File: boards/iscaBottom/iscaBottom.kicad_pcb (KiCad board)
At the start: 2 copper layers, 178.5 x 157 mm, 44 parts, among them J1 CONN_01X36, J2 CONN_01X36, J3 CONN_01X36

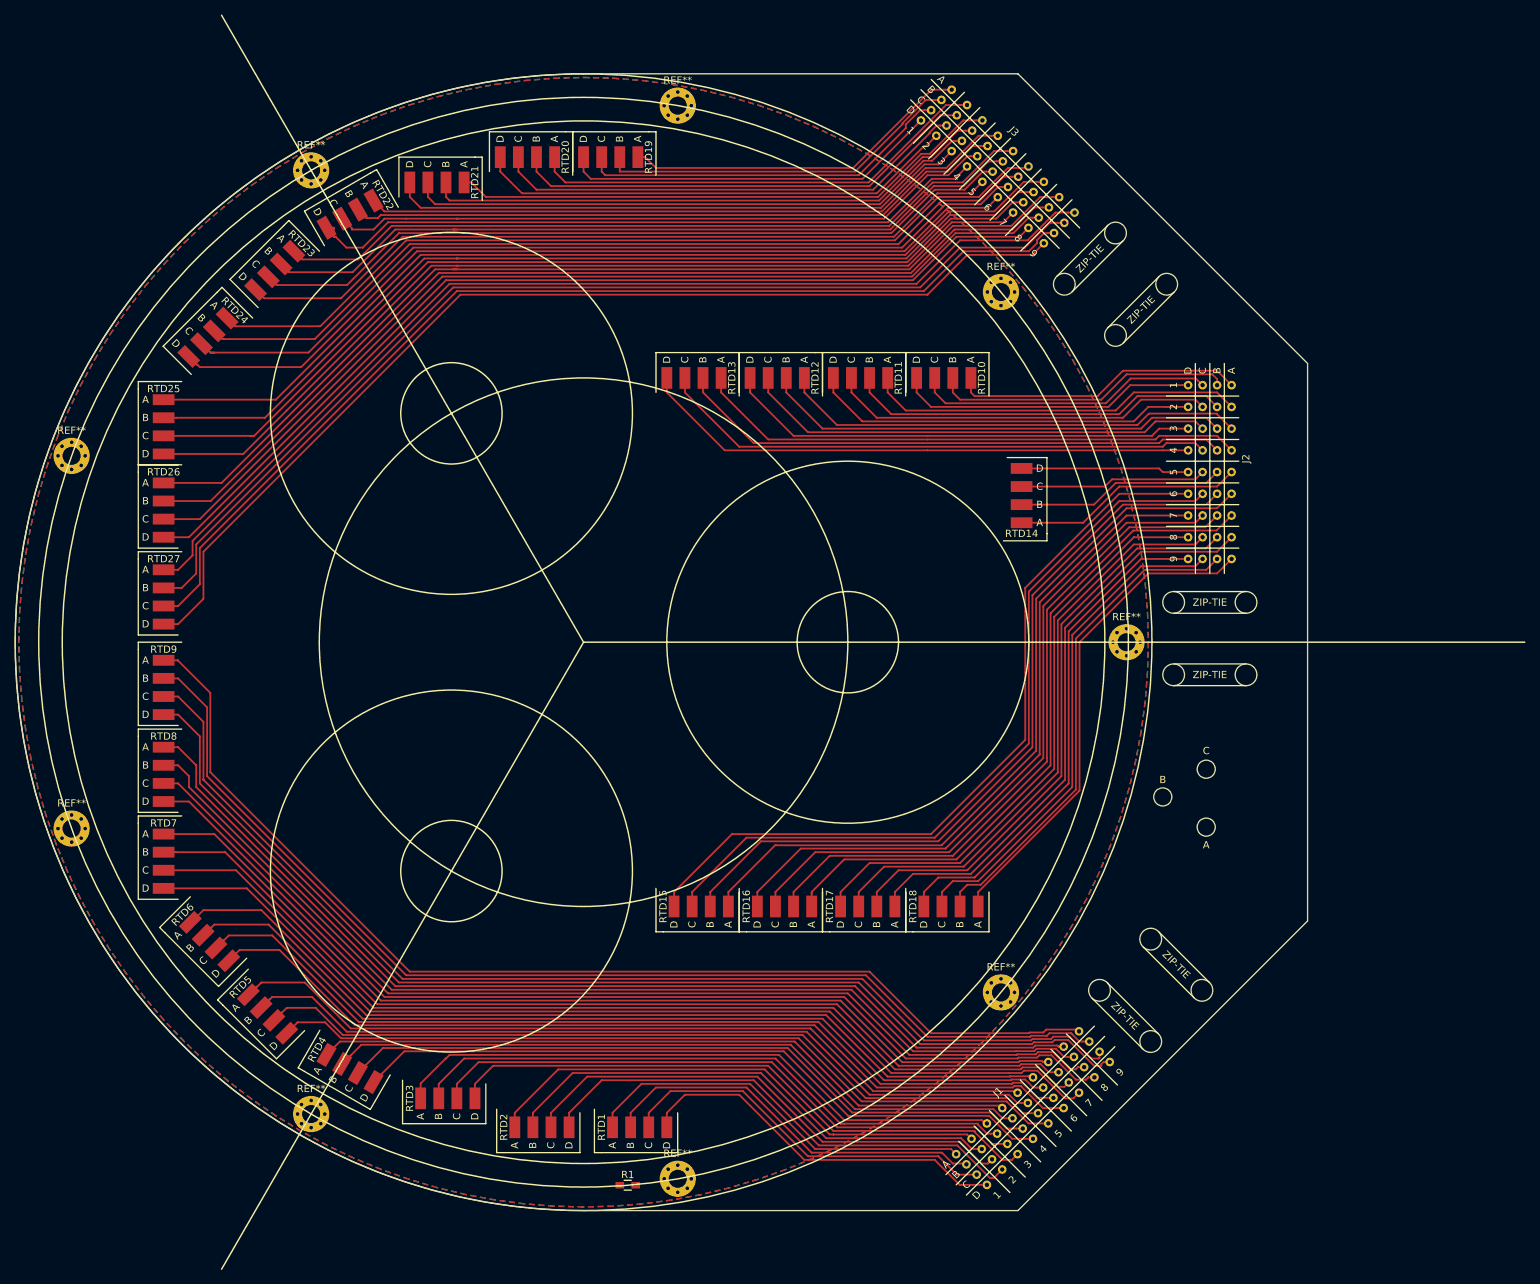
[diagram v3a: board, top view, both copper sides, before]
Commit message: addressed all the errors
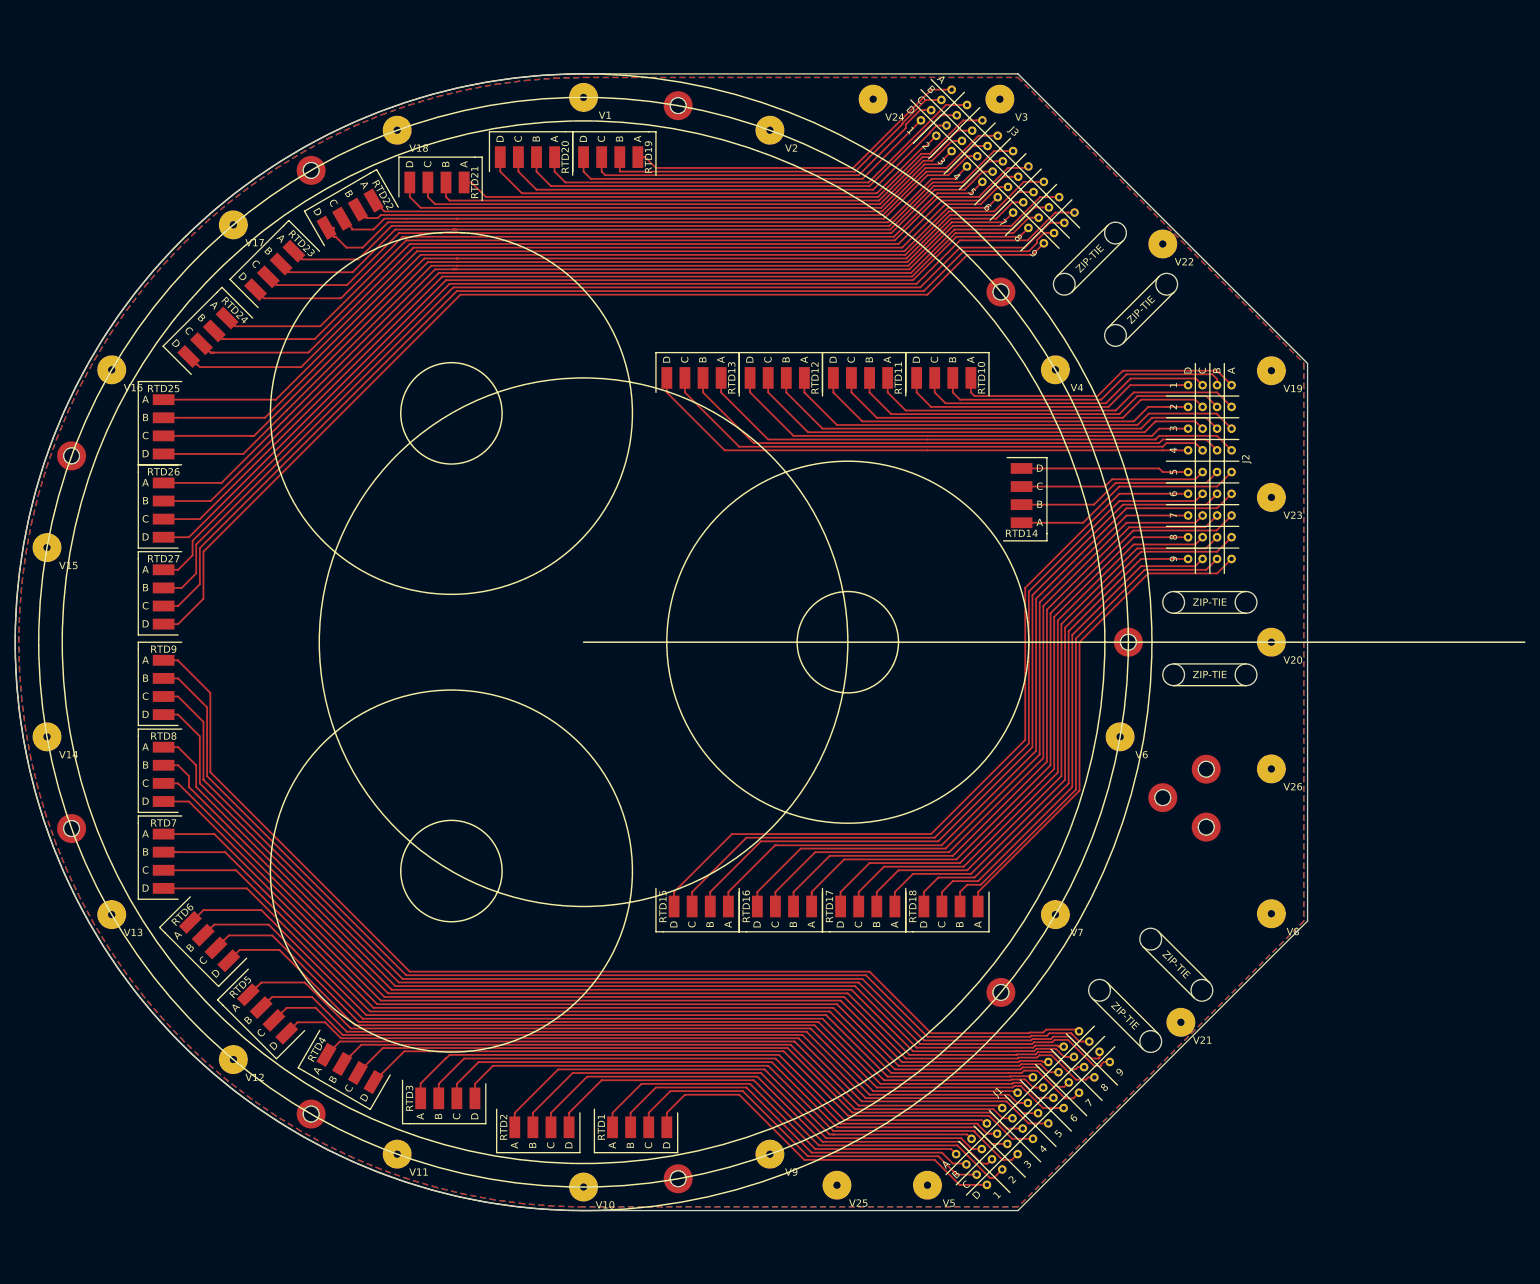
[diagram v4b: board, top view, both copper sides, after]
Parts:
- removed A: MountingHole_2.5mm_Pad_Via, Mounting_Holes:MountingHole_2.5mm
- removed B, C: MountingHole_2.5mm, Mounting_Holes:MountingHole_2.5mm
- removed R1: 0, Resistors_SMD:R_0603_HandSoldering
- removed REF** (x9): MountingHole_2.5mm_Pad_Via, Mounting_Holes:MountingHole_2.5mm_Pad_Via
- added A1: MontingHole_SinkOneSide, footprints:MountingHoleM2_2.2mm_oneSided, F.Cu at (236.0, 125.5)
- added B1: MontingHole_SinkOneSide, footprints:MountingHoleM2_2.2mm_oneSided, F.Cu at (230.0, 121.5)
- added C1: MontingHole_SinkOneSide, footprints:MountingHoleM2_2.2mm_oneSided, F.Cu at (236.0, 117.5)
- added M1: MontingHole_SinkOneSide, footprints:MountingHoleM2_2.2mm_oneSided, F.Cu at (163.1, 25.9)
- added M2: MontingHole_SinkOneSide, footprints:MountingHoleM2_2.2mm_oneSided, F.Cu at (207.6, 51.6)
- added M3: MontingHole_SinkOneSide, footprints:MountingHoleM2_2.2mm_oneSided, F.Cu at (225.2, 100.0)
- added M4: MontingHole_SinkOneSide, footprints:MountingHoleM2_2.2mm_oneSided, F.Cu at (207.6, 148.4)
- added M5: MontingHole_SinkOneSide, footprints:MountingHoleM2_2.2mm_oneSided, F.Cu at (163.1, 174.1)
- added M6: MontingHole_SinkOneSide, footprints:MountingHoleM2_2.2mm_oneSided, F.Cu at (112.4, 165.2)
- added M7: MontingHole_SinkOneSide, footprints:MountingHoleM2_2.2mm_oneSided, F.Cu at (79.3, 125.7)
- added M8: MontingHole_SinkOneSide, footprints:MountingHoleM2_2.2mm_oneSided, F.Cu at (79.3, 74.3)
- added M9: MontingHole_SinkOneSide, footprints:MountingHoleM2_2.2mm_oneSided, F.Cu at (112.4, 34.8)
- added V1: ViaGrounding, footprints:GroundingVia, F.Cu at (150.0, 24.8)
- added V10: ViaGrounding, footprints:GroundingVia, F.Cu at (150.0, 175.2)
- added V11: ViaGrounding, footprints:GroundingVia, F.Cu at (124.3, 170.7)
- added V12: ViaGrounding, footprints:GroundingVia, F.Cu at (101.6, 157.6)
- added V13: ViaGrounding, footprints:GroundingVia, F.Cu at (84.8, 137.6)
- added V14: ViaGrounding, footprints:GroundingVia, F.Cu at (75.9, 113.1)
- added V15: ViaGrounding, footprints:GroundingVia, F.Cu at (75.9, 86.9)
- added V16: ViaGrounding, footprints:GroundingVia, F.Cu at (84.8, 62.4)
- added V17: ViaGrounding, footprints:GroundingVia, F.Cu at (101.6, 42.4)
- added V18: ViaGrounding, footprints:GroundingVia, F.Cu at (124.3, 29.3)
- added V19: ViaGrounding, footprints:GroundingVia, F.Cu at (245.0, 62.5)
- added V2: ViaGrounding, footprints:GroundingVia, F.Cu at (175.7, 29.3)
- added V20: ViaGrounding, footprints:GroundingVia, F.Cu at (245.0, 100.0)
- added V21: ViaGrounding, footprints:GroundingVia, F.Cu at (232.5, 152.5)
- added V22: ViaGrounding, footprints:GroundingVia, F.Cu at (230.0, 45.0)
- added V23: ViaGrounding, footprints:GroundingVia, F.Cu at (245.0, 80.0)
- added V24: ViaGrounding, footprints:GroundingVia, F.Cu at (190.0, 25.0)
- added V25: ViaGrounding, footprints:GroundingVia, F.Cu at (185.0, 175.0)
- added V26: ViaGrounding, footprints:GroundingVia, F.Cu at (245.0, 117.5)
- added V3: ViaGrounding, footprints:GroundingVia, F.Cu at (207.5, 25.0)
- added V4: ViaGrounding, footprints:GroundingVia, F.Cu at (215.2, 62.4)
- added V5: ViaGrounding, footprints:GroundingVia, F.Cu at (197.5, 175.0)
- added V6: ViaGrounding, footprints:GroundingVia, F.Cu at (224.1, 113.1)
- added V7: ViaGrounding, footprints:GroundingVia, F.Cu at (215.2, 137.6)
- added V8: ViaGrounding, footprints:GroundingVia, F.Cu at (245.0, 137.5)
- added V9: ViaGrounding, footprints:GroundingVia, F.Cu at (175.7, 170.7)
- moved G*** 18.7 mm to (143.0, 80.6)
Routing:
- added copper zone on B.Cu, net /GND
- added copper zone on F.Cu, net /GND
- removed copper zone on B.Cu, net (none)
- removed copper zone on F.Cu, net /shield
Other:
- board text added: "1"
- board text added: "2"
- board text added: "3"
